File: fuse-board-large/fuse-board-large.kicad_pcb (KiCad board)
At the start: 2 copper layers, 106 x 152 mm, 26 parts, among them J1 Anderson_two_redblack, J10 Anderson_two_redblack, J11 Anderson_two_redblack, J2 Anderson_two_redblack, J3 Anderson_two_redblack, J4 Anderson_two_redblack, J5 Anderson_two_redblack, J6 Anderson_two_redblack, J7 Anderson_two_redblack, J8 Anderson_two_redblack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

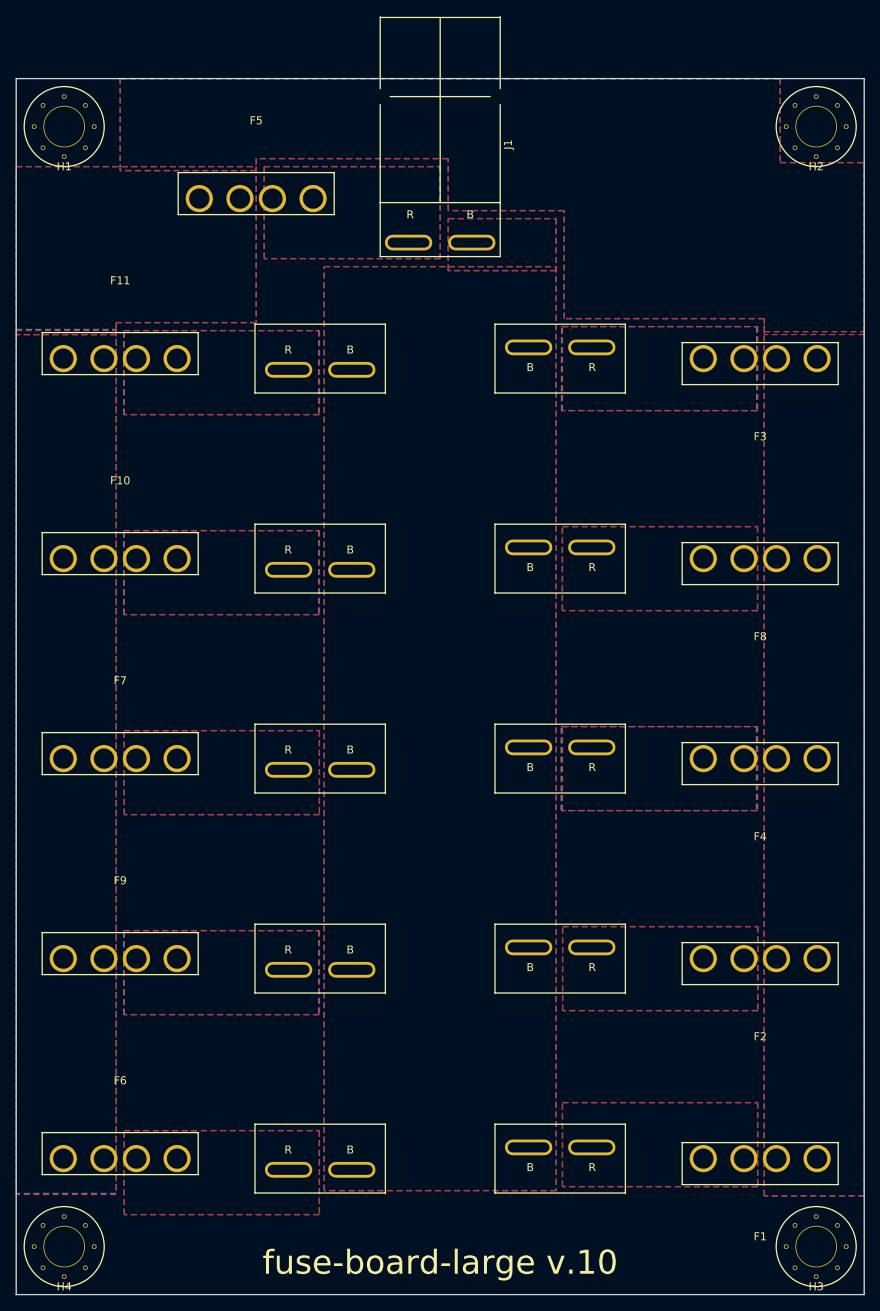
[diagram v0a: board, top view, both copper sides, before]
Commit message: fuse-board-large v1.1:
- Update straight Anderson footprint for fixed silk, bigger copper ring
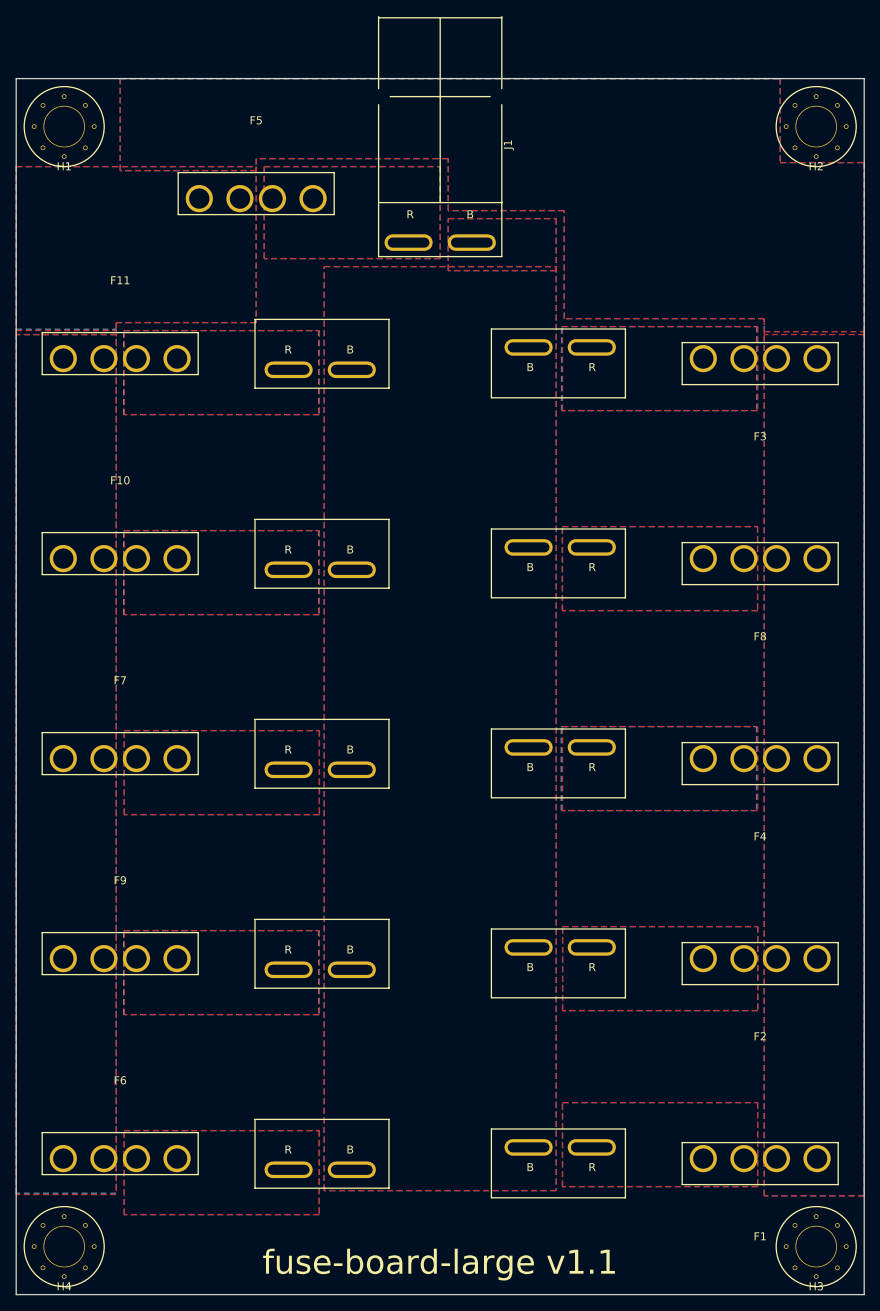
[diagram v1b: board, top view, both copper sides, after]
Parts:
- J1: footprint homebrew:Anderson_1337G3_right_angle_bottom_two -> homebrew:Anderson_1336G1_right_angle_bottom_two
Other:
- board text added: "fuse-board-large v1.1"
- board text removed: "fuse-board-large v.10"
